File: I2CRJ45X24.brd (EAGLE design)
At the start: 275 x 50 mm, 123 parts, among them IC1 MCP23017SO, IC2 MCP23017SO, IC3 MCP23017SO, IC4 MCP23017SO, IC5 MCP23017SO, IC6 MCP23017SO, J1 RJ45-X8, J2 RJ45-X8, J3 RJ45-X8, J5 M06-PIN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

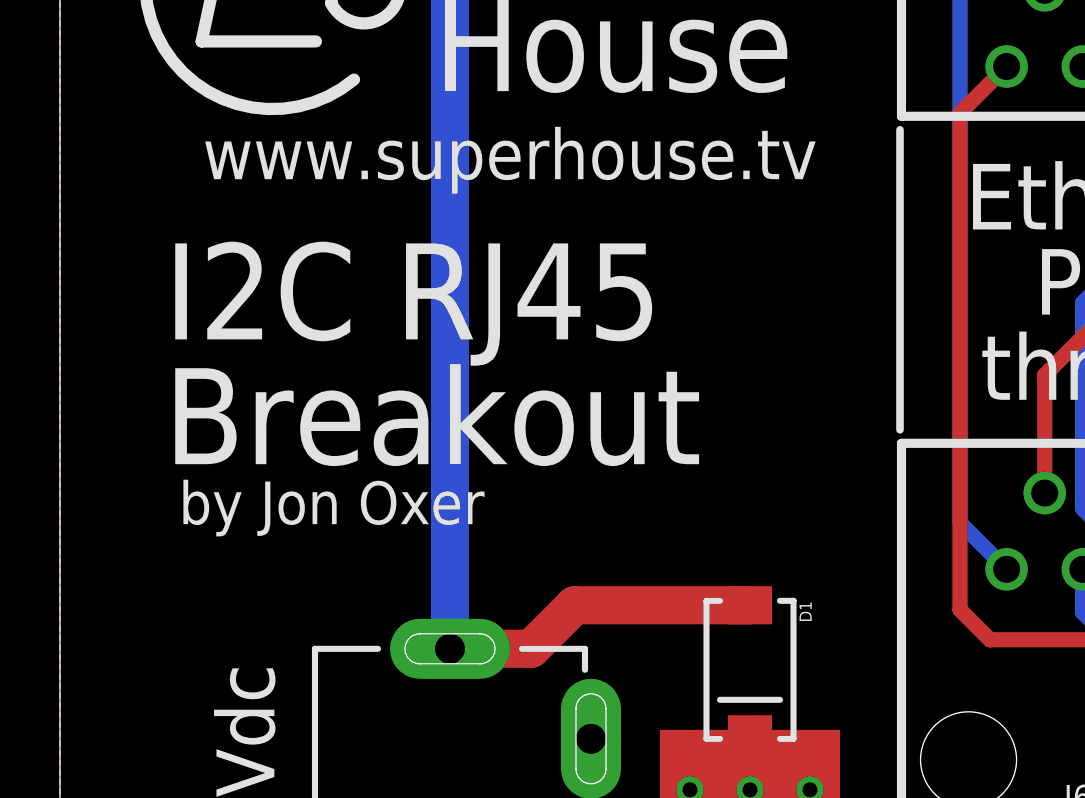
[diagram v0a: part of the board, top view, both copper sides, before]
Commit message: Board and schematic labelling
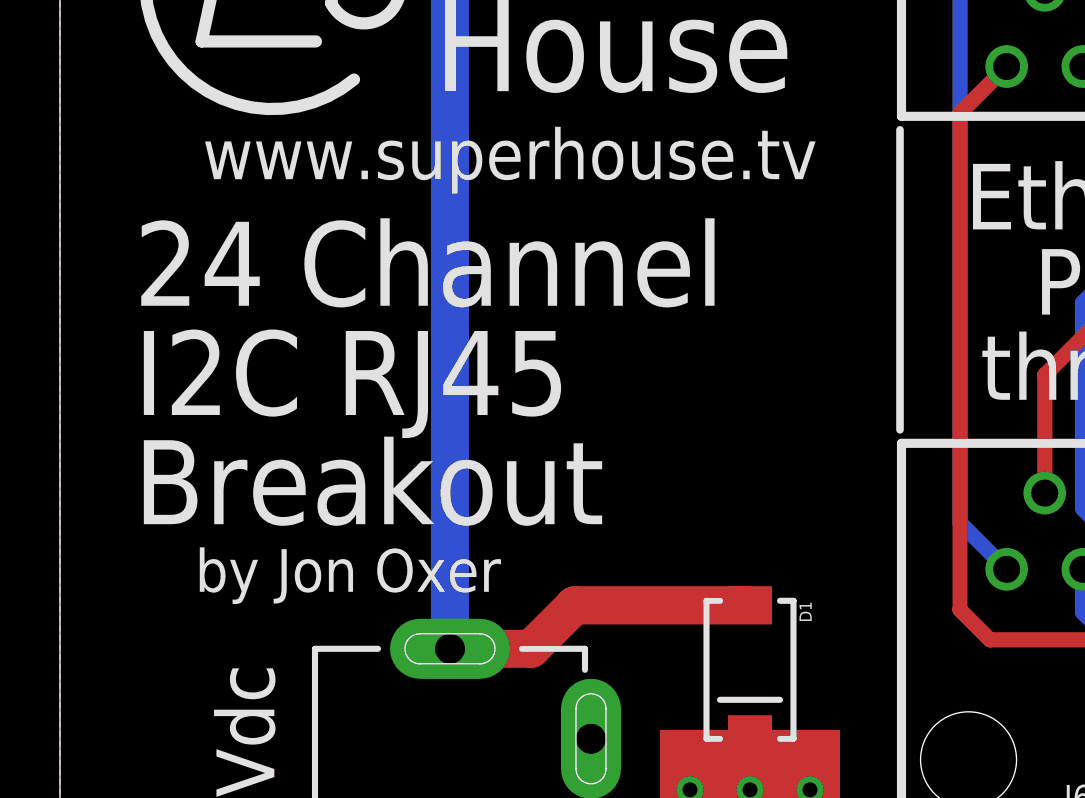
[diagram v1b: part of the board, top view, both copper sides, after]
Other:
- board text added: "24 Channel I2C RJ45 Breakout"
- board text removed: "I2C RJ45 Breakout"
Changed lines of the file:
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@@
 <text x="12.455" y="32.854" size="3.1" layer="21" font="vector" ratio="17" distance="30" align="center-left">Super
 House</text>
-<text x="3.455" y="16.854" size="3.2" layer="21" font="vector" ratio="17" distance="30">I2C RJ45
+<text x="2.455" y="14.854" size="2.8" layer="21" font="vector" ratio="17" distance="30">24 Channel
+I2C RJ45
 Breakout</text>
-<text x="3.955" y="14.854" size="1.4224" layer="21" font="vector" ratio="17" distance="30">by Jon Oxer</text>
+<text x="4.5" y="12.6" size="1.4224" layer="21" font="vector" ratio="17" distance="30">by Jon Oxer</text>
 <text x="193.455" y="34.854" size="1.6764" layer="22" font="vector" ratio="17" distance="30" rot="MR0">Copyright 2019 SuperHouse Automation Pty Ltd
 Released under the terms

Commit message: Added fiducials and optimised GND pathways
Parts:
- added FID1, FID2, FID3: FIDUCIAL1X2.5, freetronics:FIDUCIAL-1X2.5
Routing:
- net SCL: track 137.0 -> 228.5 mm, vias 5 -> 8
- net SDA: track 126.9 -> 216.6 mm, vias 4 -> 7
- net VCC: track 231.3 -> 311.8 mm, vias 1 -> 2
- net !INT: track 344.9 -> 392.3 mm, vias 0 -> 6
- net GND: track 23.7 -> 6.00 mm, vias 7 -> 4

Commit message: Final routing, plus ERC and DRC for v1.0 release
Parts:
- D1: value (none) -> SS56
- FID1, FID2, FID3: device freetronics:FIDUCIAL-1X2.5 -> SuperHouse-Symbols:FIDUCIAL-1X2.5
- J4: value (none) -> POWER
- moved J7 5.00 mm to (36.0, 44.0)
- moved FID1 3.00 mm to (34.5, 46.5)
- moved J6 2.00 mm to (36.0, 5.00)
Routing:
- net N$10: track 23.4 -> 30.4 mm
- net N$9: track 21.2 -> 28.2 mm
- net N$6: track 14.7 -> 21.7 mm
- net N$5: track 27.8 -> 34.8 mm
- net N$4: track 16.9 -> 23.9 mm
- net N$3: track 33.1 -> 40.1 mm
- net N$12: track 36.1 -> 43.1 mm
- net N$11: track 32.4 -> 39.4 mm
- net SCL: track 228.5 -> 221.9 mm
